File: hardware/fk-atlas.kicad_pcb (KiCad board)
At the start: 2 copper layers, 88.4 x 80.3 mm, 136 parts, among them J1 CONN-HDR-2x5, J2 MICRO-USB, J201 CONN_01X02, J3 Conn_01x02, J301 CONN_01X02, J4 Conn_01x09, J401 CONN_01X02, J5 Conn_01x05, J501 CONN_01X02, J601 CONN_01X02, M1 MOUNT_HOLE, M2 MOUNT_HOLE, M3 MOUNT_HOLE, M4 MOUNT_HOLE, M5 FIDUCIAL, M6 FIDUCIAL, M7 FIDUCIAL, P2 ATLAS_EC_PROBE, P3 ATLAS_RTD_PROBE, P4 ATLAS_PH_PROBE, P5 ATLAS_DO_PROBE, P6 ATLAS_ORP_PROBE, Q1 2N7002LT1G, Q2 2N7002LT1G, Q3 2N7002LT1G, Q4 2N7002LT1G, Q5 2N7002LT1G, SW1 SPNO, U1 S25FL1xxK0XM, U2 ATSAMD21G18A-AU, U201 ADM3260, U202 ATLAS_EC, U3 MCP1700T-3302E/MB, U301 ADM3260, U302 ATLAS_RTD, U401 ADM3260, U402 ATLAS_PH, U501 ADM3260, U502 ATLAS_DO, U601 ADM3260, U602 ATLAS_ORP, Y1 FC-135

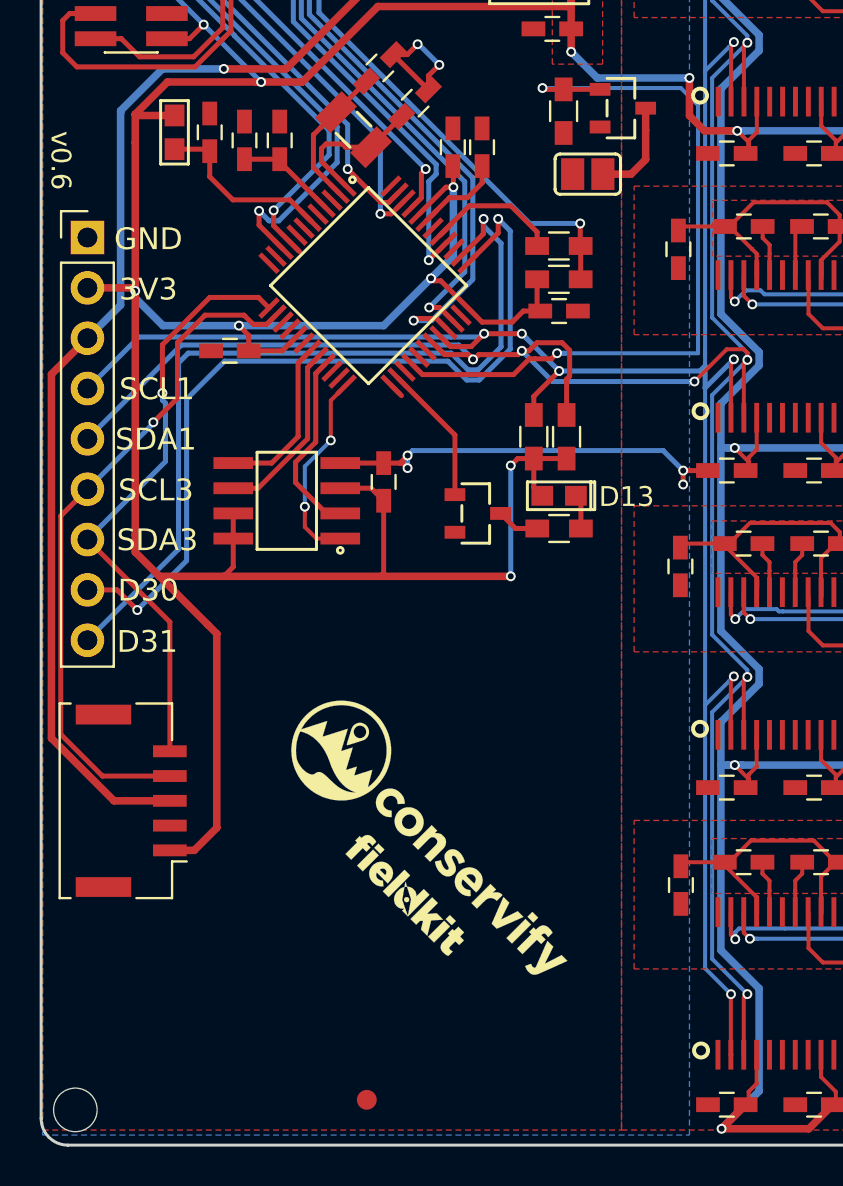
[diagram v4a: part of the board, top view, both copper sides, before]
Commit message: Add pressure sensor connector. Going to use the connectors we used before.
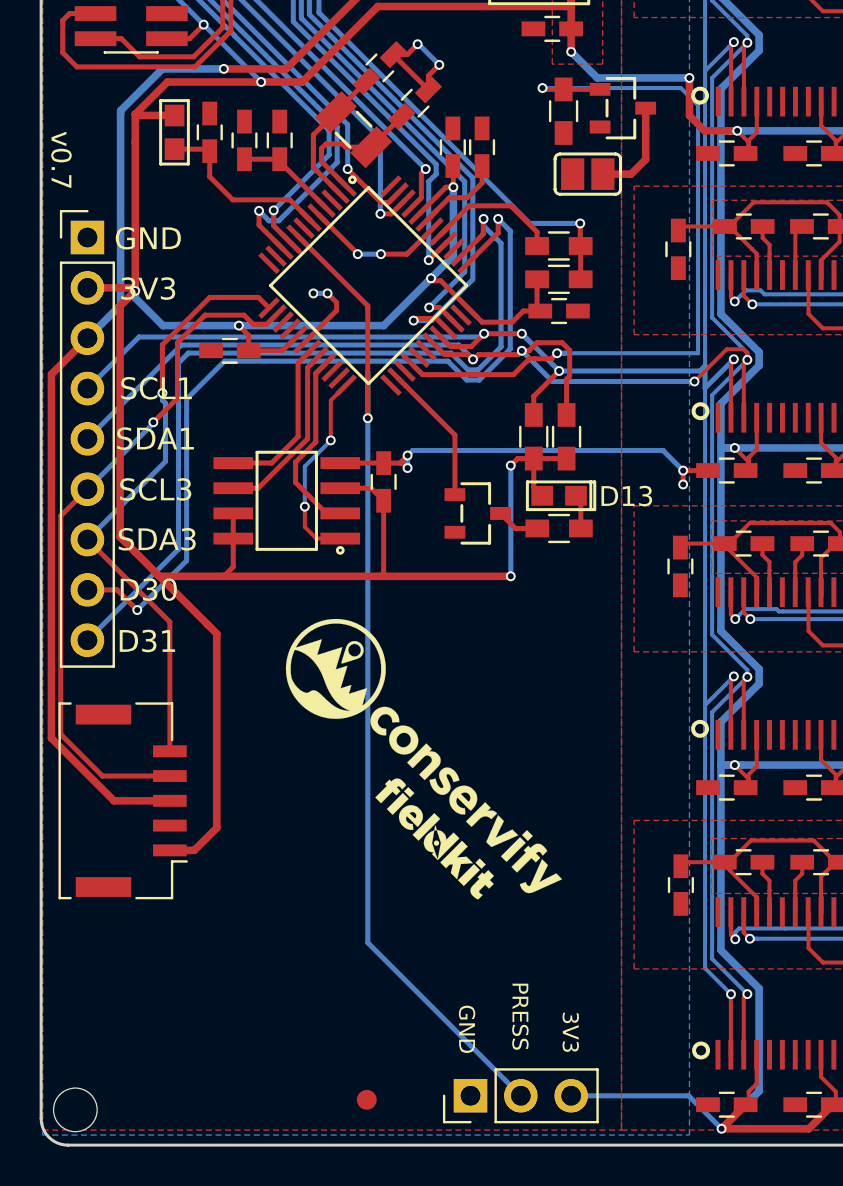
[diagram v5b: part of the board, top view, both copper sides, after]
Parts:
- added J6: Conn_01x03, Socket_Strips:Socket_Strip_Straight_1x03_Pitch2.54mm, F.Cu at (137.4, 135.2)
- moved G*** 4.13 mm to (135.2, 118.3)
- moved G*** 3.22 mm to (135.7, 122.1)
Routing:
- net /A2: track 0.00 -> 50.5 mm, vias 0 -> 1
- net GND: track 25.0 -> 36.3 mm, vias 11 -> 15
- net +3V3: track 352.8 -> 361.7 mm
- net /D11: track 0.75 -> 0.00 mm
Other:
- board text added: "PRESS"
- board text added: "v0.7"
- board text removed: "v0.6"
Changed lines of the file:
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@@
 (kicad_pcb (version 4) (host pcbnew 4.0.7-e2-6376~58~ubuntu16.04.1)
   (general
-    (links 358)
+    (links 361)
     (no_connects 0)
-    (area 112.513076 55.0796 223.731401 140.0924)
+    (area 115.672799 57.328999 204.214801 137.743001)
     (thickness 1.6)
-    (drawings 31)
-    (tracks 1272)
+    (drawings 34)
+    (tracks 1294)
     (zones 0)
-    (modules 136)
+    (modules 137)
     (nets 120)
   )
@@
   )
   (module conservify:conservify_text_negative_4000 (layer F.Cu)
-    (at 135.501861 122.383347 315)
+    (at 135.2296 118.2624 315)
     (fp_text reference G*** (at 0 0 315) (layer F.SilkS) hide
       (effects (font (thickness 0.3)))
@@
   )
   (module conservify:fk_negative_2500 (layer F.Cu)
-    (at 134.181061 124.974147 315)
+    (at 135.6868 122.1232 315)
     (fp_text reference G*** (at 0 0 315) (layer F.SilkS) hide
       (effects (font (thickness 0.3)))
@@
     )
   )
+  (module Socket_Strips:Socket_Strip_Straight_1x03_Pitch2.54mm (layer F.Cu)
+    (at 137.414 135.1788 90)
+    (descr "Through hole straight socket strip, 1x03, 2.54mm pitch, single row")
+    (tags "Through hole socket strip THT 1x03 2.54mm single row")
+    (fp_text reference J6 (at 0 -2.33 90) (layer F.SilkS) hide
+      (effects (font (size 1 1) (thickness 0.15)))
+    )
+    (fp_text value Conn_01x03 (at 0 7.41 90) (layer F.Fab)
+      (effects (font (size 1 1) (thickness 0.15)))
+    )
+    (fp_line (start -1.27 -1.27) (end -1.27 6.35) (layer F.Fab) (width 0.1))
+    (fp_line (start -1.27 6.35) (end 1.27 6.35) (layer F.Fab) (width 0.1))
+    (fp_line (start 1.27 6.35) (end 1.27 -1.27) (layer F.Fab) (width 0.1))
+    (fp_line (start 1.27 -1.27) (end -1.27 -1.27) (layer F.Fab) (width 0.1))
+    (fp_line (start -1.33 1.27) (end -1.33 6.41) (layer F.SilkS) (width 0.12))
+    (fp_line (start -1.33 6.41) (end 1.33 6.41) (layer F.SilkS) (width 0.12))
+    (fp_line (start 1.33 6.41) (end 1.33 1.27) (layer F.SilkS) (width 0.12))
+    (fp_line (start 1.33 1.27) (end -1.33 1.27) (layer F.SilkS) (width 0.12))
+    (fp_line (start -1.33 0) (end -1.33 -1.33) (layer F.SilkS) (width 0.12))
+    (fp_line (start -1.33 -1.33) (end 0 -1.33) (layer F.SilkS) (width 0.12))
+    (fp_line (start -1.8 -1.8) (end -1.8 6.85) (layer F.CrtYd) (width 0.05))
+    (fp_line (start -1.8 6.85) (end 1.8 6.85) (layer F.CrtYd) (width 0.05))
+    (fp_line (start 1.8 6.85) (end 1.8 -1.8) (layer F.CrtYd) (width 0.05))
+    (fp_line (start 1.8 -1.8) (end -1.8 -1.8) (layer F.CrtYd) (width 0.05))
+    (fp_text user %R (at 0 -2.33 90) (layer F.Fab)
+      (effects (font (size 1 1) (thickness 0.15)))
+    )
+    (pad 1 thru_hole rect (at 0 0 90) (size 1.7 1.7) (drill 1) (layers *.Cu *.Mask)
+      (net 1 GND))
+    (pad 2 thru_hole oval (at 0 2.54 90) (size 1.7 1.7) (drill 1) (layers *.Cu *.Mask)
+      (net 80 /A2))
+    (pad 3 thru_hole oval (at 0 5.08 90) (size 1.7 1.7) (drill 1) (layers *.Cu *.Mask)
+      (net 2 +3V3))
+    (model ${KISYS3DMOD}/Socket_Strips.3dshapes/Socket_Strip_Straight_1x03_Pitch2.54mm.wrl
+      (at (xyz 0 -0.1 0))
+      (scale (xyz 1 1 1))
+      (rotate (xyz 0 0 270))
+    )
+  )
+  (gr_text PRESS (at 139.9032 131.1656 270) (layer F.SilkS)
+    (effects (font (size 0.8 0.8) (thickness 0.2)))
+  )
+  (gr_text GND (at 137.2108 131.826 270) (layer F.SilkS)
+    (effects (font (size 0.8 0.8) (thickness 0.2)))
+  )
+  (gr_text 3V3 (at 142.4432 131.9784 270) (layer F.SilkS)
+    (effects (font (size 0.8 0.8) (thickness 0.2)))
+  )
   (gr_text D13 (at 145.288 104.9528) (layer F.SilkS)
     (effects (font (size 1 1) (thickness 0.2)))
@@
     (effects (font (size 1.5 1.5) (thickness 0.25)))
   )
-  (gr_text v0.6 (at 116.7384 87.9856 270) (layer F.SilkS)
+  (gr_text v0.7 (at 116.7384 87.9856 270) (layer F.SilkS)
     (effects (font (size 1 1) (thickness 0.2)))
   )
@@
   (gr_line (start 204.1398 58.7502) (end 204.1398 136.3218) (layer Edge.Cuts) (width 0.15))
   (gr_line (start 117.094 57.404) (end 202.7936 57.404) (layer Edge.Cuts) (width 0.15))
+  (segment (start 130.2004 94.6912) (end 129.4892 94.6912) (width 0.254) (layer B.Cu) (net 1))
+  (via (at 129.4892 94.6912) (size 0.5) (drill 0.3) (layers F.Cu B.Cu) (net 1))
+  (segment (start 129.017809 97.196638) (end 130.6576 95.556847) (width 0.254) (layer F.Cu) (net 1))
+  (segment (start 130.6576 95.556847) (end 130.6576 95.1484) (width 0.254) (layer F.Cu) (net 1))
+  (segment (start 130.6576 95.1484) (end 130.2004 94.6912) (width 0.254) (layer F.Cu) (net 1))
+  (via (at 130.2004 94.6912) (size 0.5) (drill 0.3) (layers F.Cu B.Cu) (net 1))
+  (segment (start 132.8928 92.71) (end 134.211553 92.71) (width 0.254) (layer F.Cu) (net 1))
+  (segment (start 134.211553 92.71) (end 135.523191 91.398362) (width 0.254) (layer F.Cu) (net 1))
+  (segment (start 131.7244 92.71) (end 132.8928 92.71) (width 0.254) (layer B.Cu) (net 1))
+  (via (at 132.8928 92.71) (size 0.5) (drill 0.3) (layers F.Cu B.Cu) (net 1))
+  (segment (start 129.724916 90.691255) (end 131.7244 92.690739) (width 0.254) (layer F.Cu) (net 1))
+  (segment (start 131.7244 92.690739) (end 131.7244 92.71) (width 0.254) (layer F.Cu) (net 1))
+  (via (at 131.7244 92.71) (size 0.5) (drill 0.3) (layers F.Cu B.Cu) (net 1))
   (segment (start 137.414 78.994) (end 139.2134 78.994) (width 0.254) (layer B.Cu) (net 1))
   (segment (start 139.2134 78.994) (end 139.3811 78.8263) (width 0.254) (layer B.Cu) (net 1))
@@
   (via (at 135.8392 83.1596) (size 0.5) (drill 0.3) (layers F.Cu B.Cu) (net 1))
   (segment (start 133.513751 82.640249) (end 135.291751 84.418249) (width 0.254) (layer F.Cu) (net 1))
+  (segment (start 119.7356 95.3262) (end 119.7356 106.9848) (width 0.381) (layer F.Cu) (net 2))
+  (segment (start 119.7356 106.9848) (end 120.4976 107.7468) (width 0.381) (layer F.Cu) (net 2))
+  (segment (start 120.4976 94.5642) (end 119.7356 95.3262) (width 0.381) (layer F.Cu) (net 2))
+  (segment (start 142.494 135.1788) (end 148.4193 135.1788) (width 0.254) (layer B.Cu) (net 2))
+  (segment (start 148.4193 135.1788) (end 150.083 136.8425) (width 0.254) (layer B.Cu) (net 2))
   (segment (start 124.6124 121.6574) (end 124.6124 111.8616) (width 0.381) (layer F.Cu) (net 2))
   (segment (start 124.6124 111.8616) (end 124.1552 111.4044) (width 0.381) (layer F.Cu) (net 2))
@@
   (via (at 139.446 108.966) (size 0.5) (drill 0.3) (layers F.Cu B.Cu) (net 2))
   (segment (start 120.4976 107.7468) (end 121.7168 108.966) (width 0.381) (layer F.Cu) (net 2))
-  (segment (start 120.4976 106.8832) (end 120.4976 107.7468) (width 0.381) (layer F.Cu) (net 2))
-  (segment (start 120.4976 94.5642) (end 120.4976 106.8832) (width 0.381) (layer F.Cu) (net 2))
   (segment (start 140.606566 103.0224) (end 140.608469 103.024303) (width 0.254) (layer F.Cu) (net 2))
   (segment (start 142.262283 103.024303) (end 140.608469 103.024303) (width 0.254) (layer F.Cu) (net 2))
@@
   (segment (start 140.773648 91.593298) (end 139.45195 90.2716) (width 0.254) (layer F.Cu) (net 77))
   (segment (start 135.876745 91.751916) (end 136.442661 91.186) (width 0.254) (layer F.Cu) (net 77))
+  (segment (start 132.2324 98.63834) (end 132.2324 100.9904) (width 0.254) (layer B.Cu) (net 80))
+  (segment (start 132.2324 100.9904) (end 132.2324 127.4572) (width 0.254) (layer B.Cu) (net 80))
+  (segment (start 132.2324 95.452417) (end 132.2324 100.9904) (width 0.254) (layer F.Cu) (net 80))
+  (via (at 132.2324 100.9904) (size 0.5) (drill 0.3) (layers F.Cu B.Cu) (net 80))
+  (segment (start 132.2324 127.4572) (end 139.954 135.1788) (width 0.254) (layer B.Cu) (net 80))
+  (segment (start 128.664255 91.751916) (end 132.2324 95.320061) (width 0.254) (layer F.Cu) (net 80))
+  (segment (start 132.2324 95.320061) (end 132.2324 95.452417) (width 0.254) (layer F.Cu) (net 80))
   (segment (start 128.7145 101.9175) (end 127.381 103.251) (width 0.254) (layer F.Cu) (net 85))
   (segment (start 127.381 103.251) (end 125.443 103.251) (width 0.254) (layer F.Cu) (net 85))
@@
   (segment (start 128.5875 104.2355) (end 130.143 105.791) (width 0.254) (layer F.Cu) (net 87))
   (segment (start 130.143 105.791) (end 130.843 105.791) (width 0.254) (layer F.Cu) (net 87))
-  (segment (start 133.9322 99.848287) (end 133.401871 99.317958) (width 0.254) (layer F.Cu) (net 90))
   (segment (start 136.628459 104.843393) (end 136.628459 101.83744) (width 0.254) (layer F.Cu) (net 91))
   (segment (start 136.628459 101.83744) (end 133.755424 98.964405) (width 0.254) (layer F.Cu) (net 91))
